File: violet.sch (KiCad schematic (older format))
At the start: 47 parts, among them J1 NEIGHBOR1, J10 Conn_01x08, J2 NEIGHBOR2, J3 NEIGHBOR1, J4 BONUS_ROW, J5 NEIGHBOR2, J6 NEIGHBOR1, J7 BONUS_ROW, J8 BONUS_ROW, J9 NEIGHBOR2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

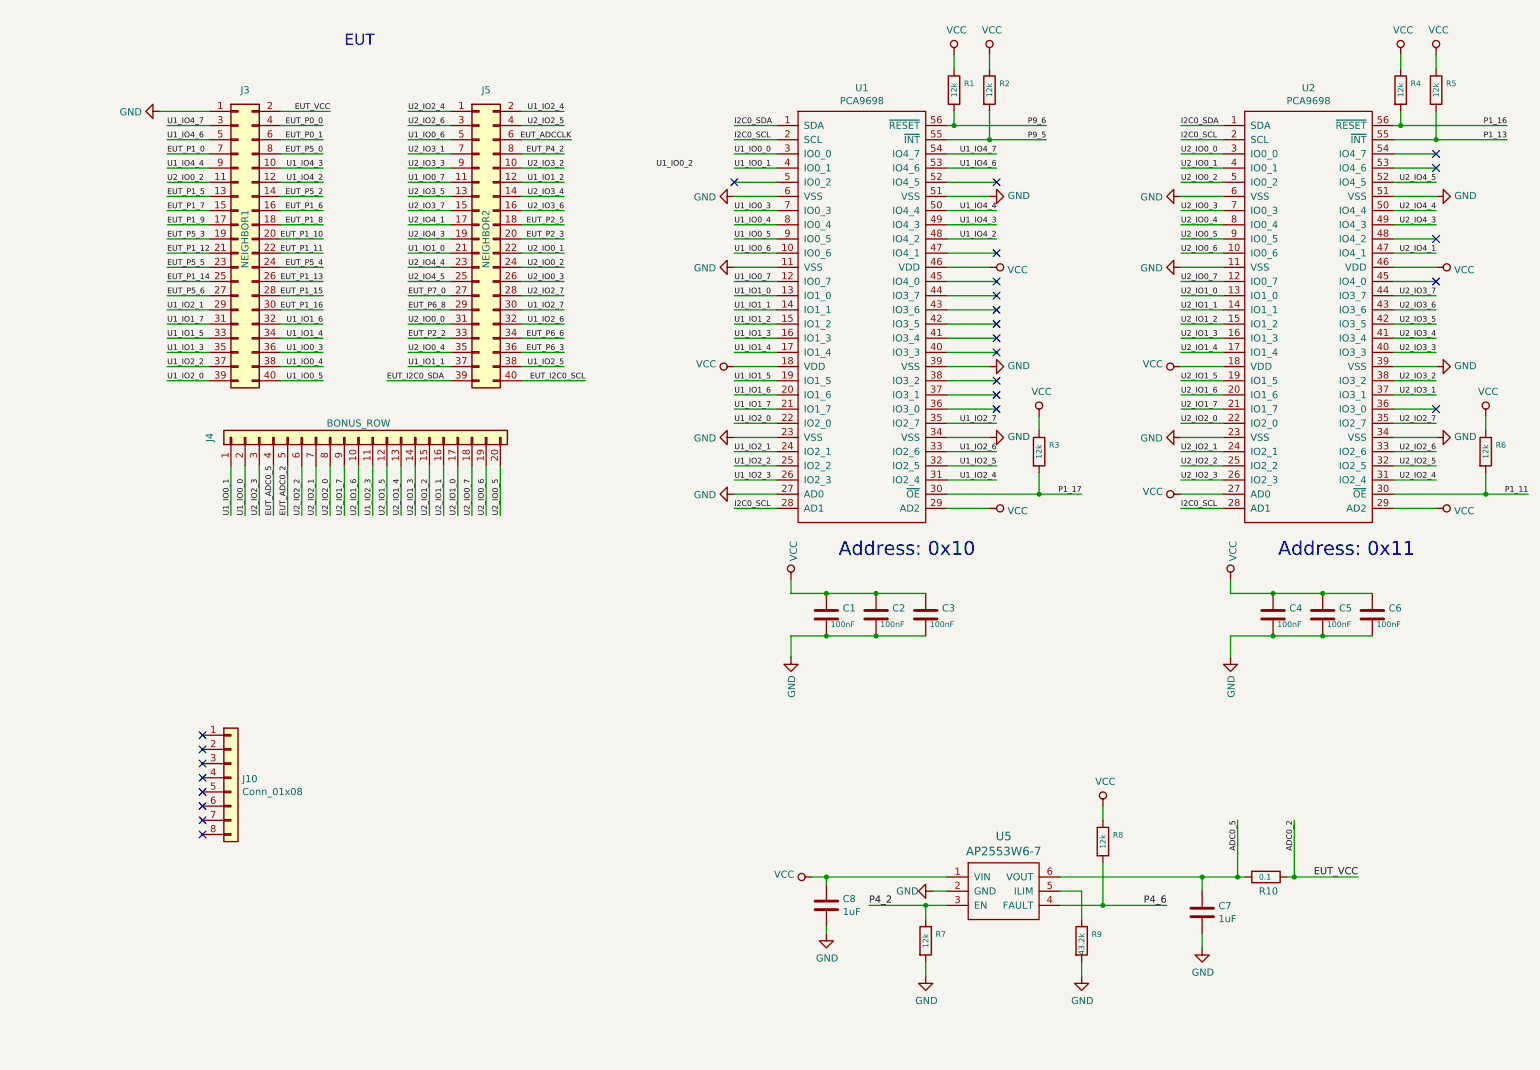
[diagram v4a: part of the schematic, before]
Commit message: Re-map I/O expanders for easier routing
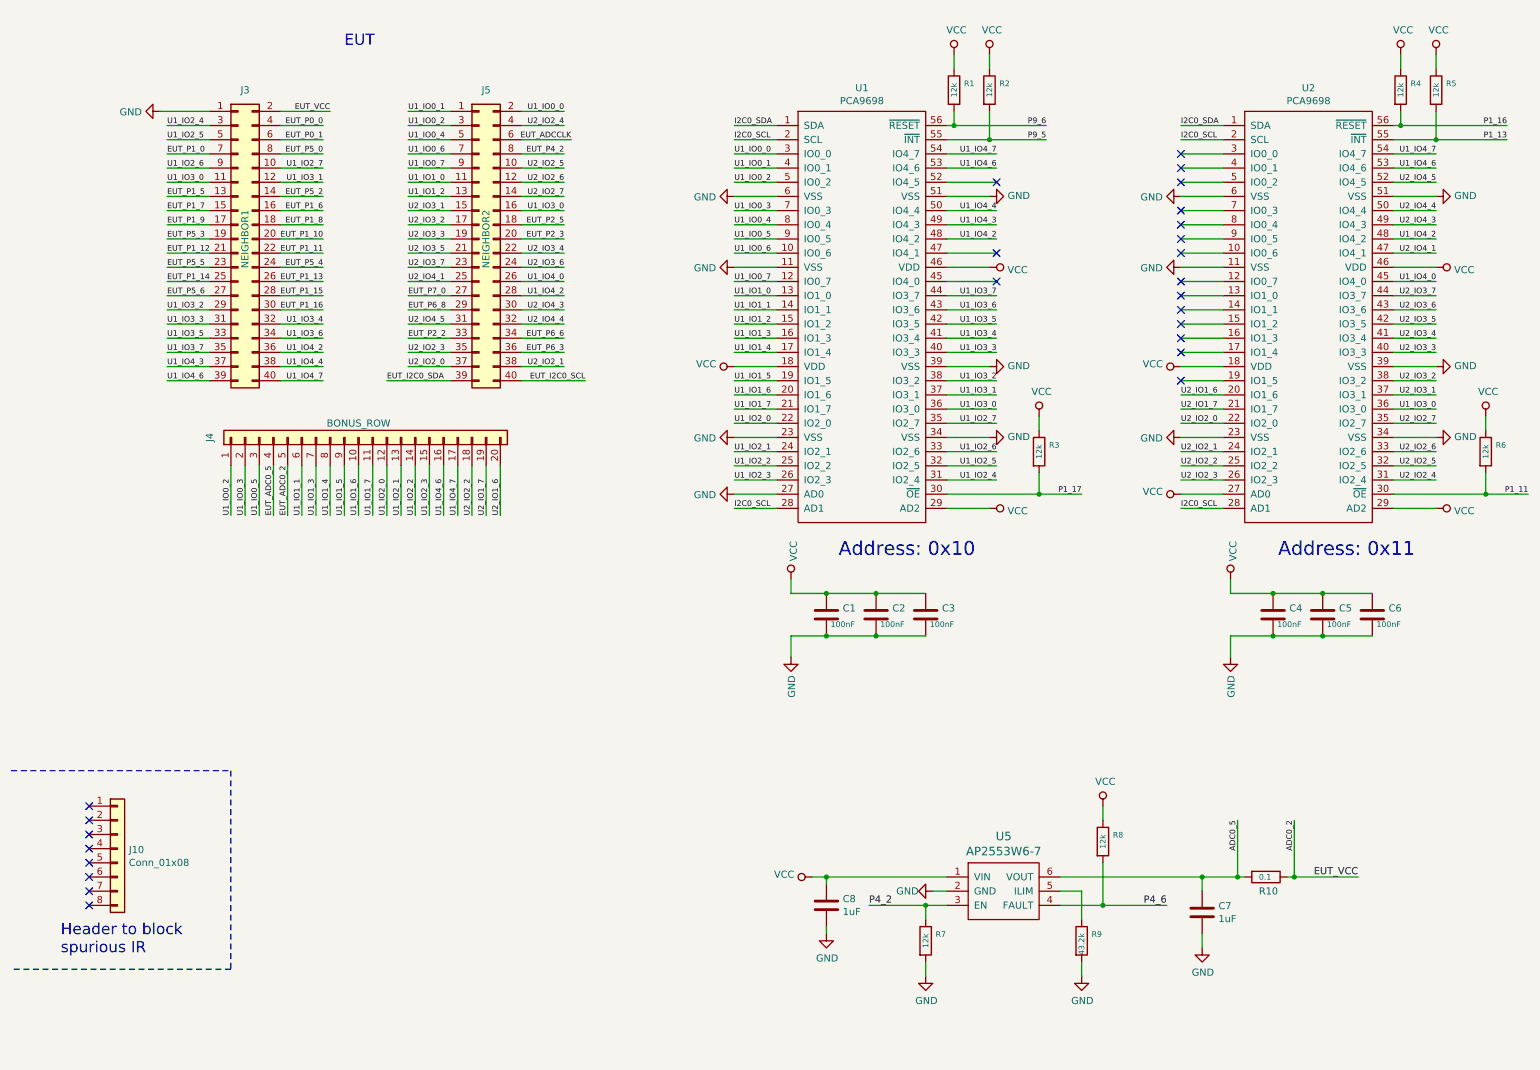
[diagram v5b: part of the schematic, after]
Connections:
- net U1_IO0_0: now also J5.2 (Pin_2); no longer J4.2 (Pin_2)
- net U1_IO0_1: now also J5.1 (Pin_1); no longer J4.1 (Pin_1)
- net U1_IO0_2: now also J4.1 (Pin_1), J5.3 (Pin_3), U1.5 (IO0_2)
- net U1_IO0_3: now also J4.2 (Pin_2); no longer J3.36 (Pin_36)
- net U1_IO0_4: now also J5.5 (Pin_5); no longer J3.38 (Pin_38)
- net U1_IO0_5: now also J4.3 (Pin_3); no longer J3.40 (Pin_40)
- net U1_IO0_6: now also J5.7 (Pin_7); no longer J5.5 (Pin_5)
- net U1_IO0_7: now also J5.9 (Pin_9); no longer J5.11 (Pin_11)
- net U1_IO1_0: now also J5.11 (Pin_11); no longer J5.21 (Pin_21)
- net U1_IO1_1: now also J4.6 (Pin_6); no longer J5.37 (Pin_37)
- net U1_IO1_2: now also J5.13 (Pin_13); no longer J5.12 (Pin_12)
- net U1_IO1_3: now also J4.7 (Pin_7); no longer J3.35 (Pin_35)
- net U1_IO1_4: now also J4.8 (Pin_8); no longer J3.34 (Pin_34)
- net U1_IO1_5: now also J4.9 (Pin_9); no longer J3.33 (Pin_33)
- net U1_IO1_6: now also J4.10 (Pin_10); no longer J3.32 (Pin_32)
- net U1_IO1_7: now also J4.11 (Pin_11); no longer J3.31 (Pin_31)
- net U1_IO2_0: now also J4.12 (Pin_12); no longer J3.39 (Pin_39)
- net U1_IO2_1: now also J4.13 (Pin_13); no longer J3.29 (Pin_29)
- net U1_IO2_2: now also J4.14 (Pin_14); no longer J3.37 (Pin_37)
- net U1_IO2_3: now also J4.15 (Pin_15); no longer J4.11 (Pin_11)
- net U1_IO2_4: now also J3.3 (Pin_3); no longer J5.2 (Pin_2)
- net U1_IO2_5: now also J3.5 (Pin_5); no longer J5.38 (Pin_38)
- net U1_IO2_6: now also J3.9 (Pin_9); no longer J5.32 (Pin_32)
- net U1_IO2_7: now also J3.10 (Pin_10); no longer J5.30 (Pin_30)
- net U1_IO4_2: now also J3.36 (Pin_36), J5.28 (Pin_28), U2.48 (IO4_2); no longer J3.12 (Pin_12)
- net U1_IO4_3: now also J3.37 (Pin_37); no longer J3.10 (Pin_10)
- net U1_IO4_4: now also J3.38 (Pin_38); no longer J3.9 (Pin_9)
- net U1_IO4_6: now also J3.39 (Pin_39), J4.16 (Pin_16), U2.53 (IO4_6); no longer J3.5 (Pin_5)
- net U1_IO4_7: now also J3.40 (Pin_40), J4.17 (Pin_17), U2.54 (IO4_7); no longer J3.3 (Pin_3)
- net U2_IO1_6: now also J4.20 (Pin_20); no longer J4.10 (Pin_10)
- net U2_IO1_7: now also J4.19 (Pin_19); no longer J4.9 (Pin_9)
- net U2_IO2_0: now also J5.37 (Pin_37); no longer J4.8 (Pin_8)
- net U2_IO2_1: now also J5.38 (Pin_38); no longer J4.7 (Pin_7)
- net U2_IO2_2: now also J4.18 (Pin_18); no longer J4.6 (Pin_6)
- net U2_IO2_3: now also J5.35 (Pin_35); no longer J4.3 (Pin_3)
- net U2_IO2_4: now also J5.4 (Pin_4); no longer J5.1 (Pin_1)
- net U2_IO2_5: now also J5.10 (Pin_10); no longer J5.4 (Pin_4)
- net U2_IO2_6: now also J5.12 (Pin_12); no longer J5.3 (Pin_3)
- net U2_IO2_7: now also J5.14 (Pin_14); no longer J5.28 (Pin_28)
- net U2_IO3_1: now also J5.15 (Pin_15); no longer J5.7 (Pin_7)
- net U2_IO3_2: now also J5.17 (Pin_17); no longer J5.10 (Pin_10)
- net U2_IO3_3: now also J5.19 (Pin_19); no longer J5.9 (Pin_9)
- net U2_IO3_4: now also J5.22 (Pin_22); no longer J5.14 (Pin_14)
- net U2_IO3_5: now also J5.21 (Pin_21); no longer J5.13 (Pin_13)
- net U2_IO3_6: now also J5.24 (Pin_24); no longer J5.16 (Pin_16)
- net U2_IO3_7: now also J5.23 (Pin_23); no longer J5.15 (Pin_15)
- net U2_IO4_1: now also J5.25 (Pin_25); no longer J5.17 (Pin_17)
- net U2_IO4_3: now also J5.30 (Pin_30); no longer J5.19 (Pin_19)
- net U2_IO4_4: now also J5.32 (Pin_32); no longer J5.23 (Pin_23)
- net U2_IO4_5: now also J5.31 (Pin_31); no longer J5.25 (Pin_25)
- net U1_IO3_0: now reaches U1.36 (IO3_0)
- net U1_IO3_0: now also J3.11 (Pin_11), J5.16 (Pin_16), U2.36 (IO3_0)
- net U1_IO3_1: now reaches U1.37 (IO3_1)
- net U1_IO3_1: now also J3.12 (Pin_12)
- net U1_IO3_2: now reaches U1.38 (IO3_2)
- net U1_IO3_2: now also J3.29 (Pin_29)
- net U1_IO3_3: now reaches U1.40 (IO3_3)
- net U1_IO3_3: now also J3.31 (Pin_31)
- net U1_IO3_4: now reaches U1.41 (IO3_4)
- net U1_IO3_4: now also J3.32 (Pin_32)
- net U1_IO3_5: now reaches U1.42 (IO3_5)
- net U1_IO3_5: now also J3.33 (Pin_33)
- net U1_IO3_6: now reaches U1.43 (IO3_6)
- net U1_IO3_6: now also J3.34 (Pin_34)
- net U1_IO3_7: now reaches U1.44 (IO3_7)
- net U1_IO3_7: now also J3.35 (Pin_35)
- net U1_IO4_0: now reaches U2.45 (IO4_0)
- net U1_IO4_0: now also J5.26 (Pin_26)
- net U2_IO0_0: no longer names the net of U2.3 (IO0_0)
- net U2_IO0_0: no longer J5.31 (Pin_31)
- net U2_IO0_1: no longer names the net of U2.4 (IO0_1)
- net U2_IO0_1: no longer J5.22 (Pin_22)
- removed net U2_IO0_2: J3.11 (Pin_11), J5.24 (Pin_24), U2.5 (IO0_2)
- net U2_IO0_3: no longer names the net of U2.7 (IO0_3)
- net U2_IO0_3: no longer J5.26 (Pin_26)
- net U2_IO0_4: no longer names the net of U2.8 (IO0_4)
- net U2_IO0_4: no longer J5.35 (Pin_35)
- net U2_IO0_5: no longer names the net of U2.9 (IO0_5)
- net U2_IO0_5: no longer J4.20 (Pin_20)
- net U2_IO0_6: no longer names the net of U2.10 (IO0_6)
- net U2_IO0_6: no longer J4.19 (Pin_19)
- net U2_IO0_7: no longer names the net of U2.12 (IO0_7)
- net U2_IO0_7: no longer J4.18 (Pin_18)
- net U2_IO1_0: no longer names the net of U2.13 (IO1_0)
- net U2_IO1_0: no longer J4.17 (Pin_17)
- net U2_IO1_1: no longer names the net of U2.14 (IO1_1)
- net U2_IO1_1: no longer J4.16 (Pin_16)
- net U2_IO1_2: no longer names the net of U2.15 (IO1_2)
- net U2_IO1_2: no longer J4.15 (Pin_15)
- net U2_IO1_3: no longer names the net of U2.16 (IO1_3)
- net U2_IO1_3: no longer J4.14 (Pin_14)
- net U2_IO1_4: no longer names the net of U2.17 (IO1_4)
- net U2_IO1_4: no longer J4.13 (Pin_13)
- net U2_IO1_5: no longer names the net of U2.19 (IO1_5)
- net U2_IO1_5: no longer J4.12 (Pin_12)
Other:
- note added: "Header to block\nspurious IR"
- moved on the sheet: J10

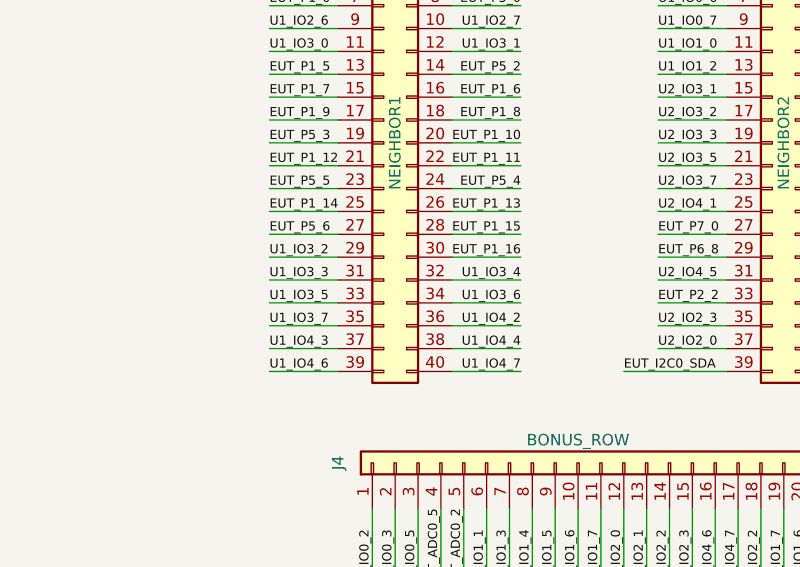
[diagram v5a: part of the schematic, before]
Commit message: Route most of U1
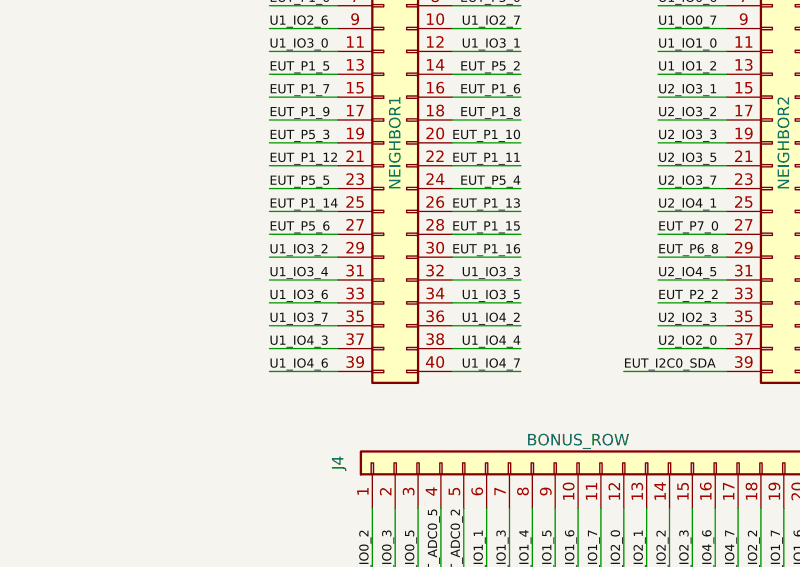
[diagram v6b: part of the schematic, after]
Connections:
- net U1_IO3_3: now also J3.32 (Pin_32); no longer J3.31 (Pin_31)
- net U1_IO3_4: now also J3.31 (Pin_31); no longer J3.32 (Pin_32)
- net U1_IO3_5: now also J3.34 (Pin_34); no longer J3.33 (Pin_33)
- net U1_IO3_6: now also J3.33 (Pin_33); no longer J3.34 (Pin_34)
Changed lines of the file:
@@
 Text Label 7450 3150 2    40   ~ 0
 U1_IO3_3
-Text Label 1600 2950 0    40   ~ 0
+Text Label 2700 2950 2    40   ~ 0
 U1_IO3_3
 Text Label 7450 3050 2    40   ~ 0
 U1_IO3_4
-Text Label 2700 2950 2    40   ~ 0
+Text Label 1600 2950 0    40   ~ 0
 U1_IO3_4
 Text Label 7450 2950 2    40   ~ 0
 U1_IO3_5
-Text Label 1600 3050 0    40   ~ 0
+Text Label 2700 3050 2    40   ~ 0
 U1_IO3_5
 Text Label 7450 2850 2    40   ~ 0
 U1_IO3_6
-Text Label 2700 3050 2    40   ~ 0
+Text Label 1600 3050 0    40   ~ 0
 U1_IO3_6
 Text Label 7450 2750 2    40   ~ 0
